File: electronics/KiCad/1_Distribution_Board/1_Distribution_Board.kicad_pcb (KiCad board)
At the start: 2 copper layers, 130 x 120 mm, 193 parts, among them CN1 HC-5264-3A, CN2 HC-5264-3A, J1 JST VH, J10 Generic 2.54mm, J11 Generic 2.54mm, J12 Conn_01x06, J13 Conn_01x10, J14 2.54-1*4P母, J15 2.54-1*4P母, J16 PM254V-11-06-H85, J17 Conn_02x08_Odd_Even, J18 PM254V-11-06-H85, J19 2.54-1*4P母, J2 JST VH, J20 2.54-1*4P母, J21 Jumper Pins, J22 Jumper Pins, J23 JST PH, J24 Generic 2.54mm, J25 Jumper Pins, J26 Jumper Pins, J27 JST PH, J28 Generic 2.54mm, J29 Jumper Pins, J3 JST VH, J30 Jumper Pins, J31 JST PH, J32 Generic 2.54mm, J33 Jumper Pins, J34 Jumper Pins, J35 JST PH, J36 Generic 2.54mm, J37 Jumper Pins, J38 Jumper Pins, J39 JST PH, J4 Conn_01x04, J40 Generic 2.54mm, J5 Generic 2.54mm, J6 Generic 2.54mm, J8 Generic 2.54mm, J9 Generic 2.54mm, M1 MountingHole_3.2mm_M3_ISO7380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, P1 Header-Female-2.54_1x8, P10 Header-Female-2.54_1x8, P11 Header-Female-2.54_1x2, P12 Header-Female-2.54_1x8, P13 Header-Female-2.54_1x8, P14 Header-Female-2.54_1x2, P15 Header-Female-2.54_1x8, P2 Header-Female-2.54_1x2, P3 Header-Female-2.54_1x8, P4 Header-Female-2.54_1x8, P5 Header-Female-2.54_1x2, P6 Header-Female-2.54_1x8, P7 Header-Female-2.54_1x8, P8 Header-Female-2.54_1x2, P9 Header-Female-2.54_1x8, Q1 DMG2305UX, Q2 AO3400A, Q3 AO3400A, Q4 AO3400A, Q5 AO3400A, U1 KH-2.54FH-1X20P-H8.5, U2 KH-2.54FH-1X20P-H8.5, U3 R-78C5.0-1.0, U4 R-78B12-2.0, U5 R-78B6.5-1.5, U6 PCA9306, U7 PCA9685PW, Y1 25MHz

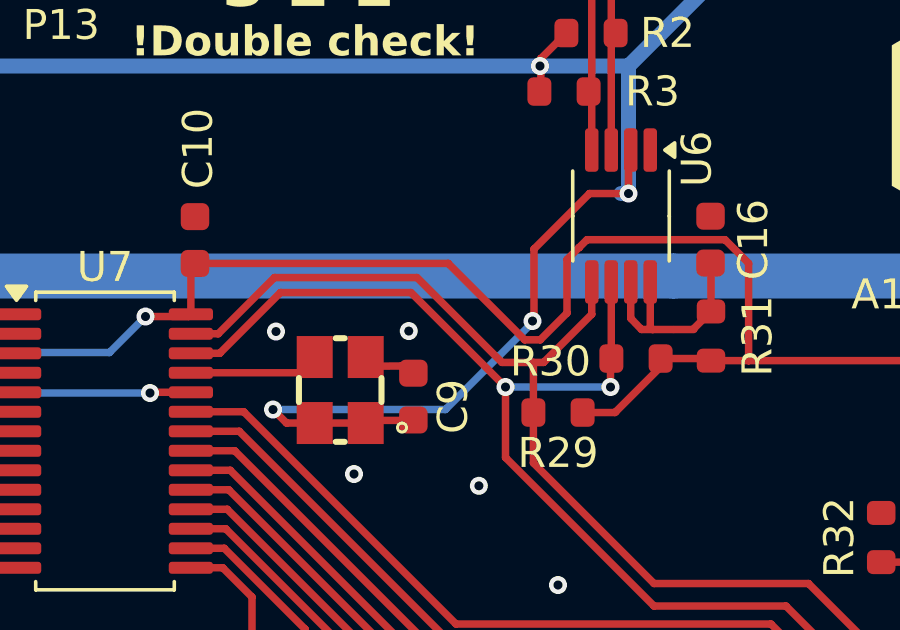
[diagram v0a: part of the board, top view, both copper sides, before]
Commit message: Fix Y1 oscillator supply routing and switch to 5V
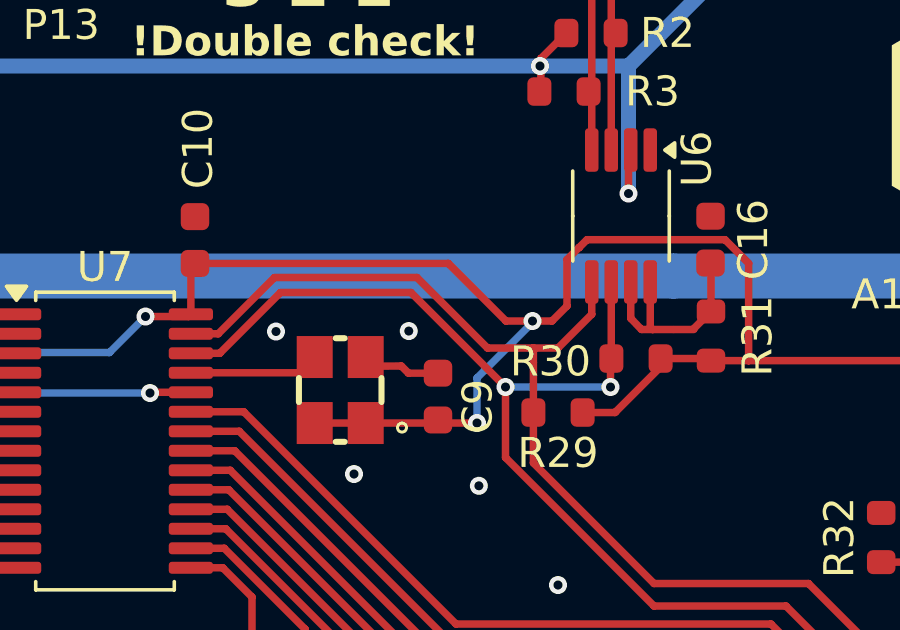
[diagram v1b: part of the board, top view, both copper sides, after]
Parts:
- moved C9 0.82 mm to (68.9, 98.5)
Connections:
- C9 pad 2: +3V3 -> VSYS
- Y1 pad 1: +3V3 -> VSYS
- Y1 pad 4: +3V3 -> VSYS
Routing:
- net +3V3: track 478.5 -> 456.8 mm, vias 19 -> 17
- net VSYS: track 170.5 -> 174.2 mm, vias 3 -> 5

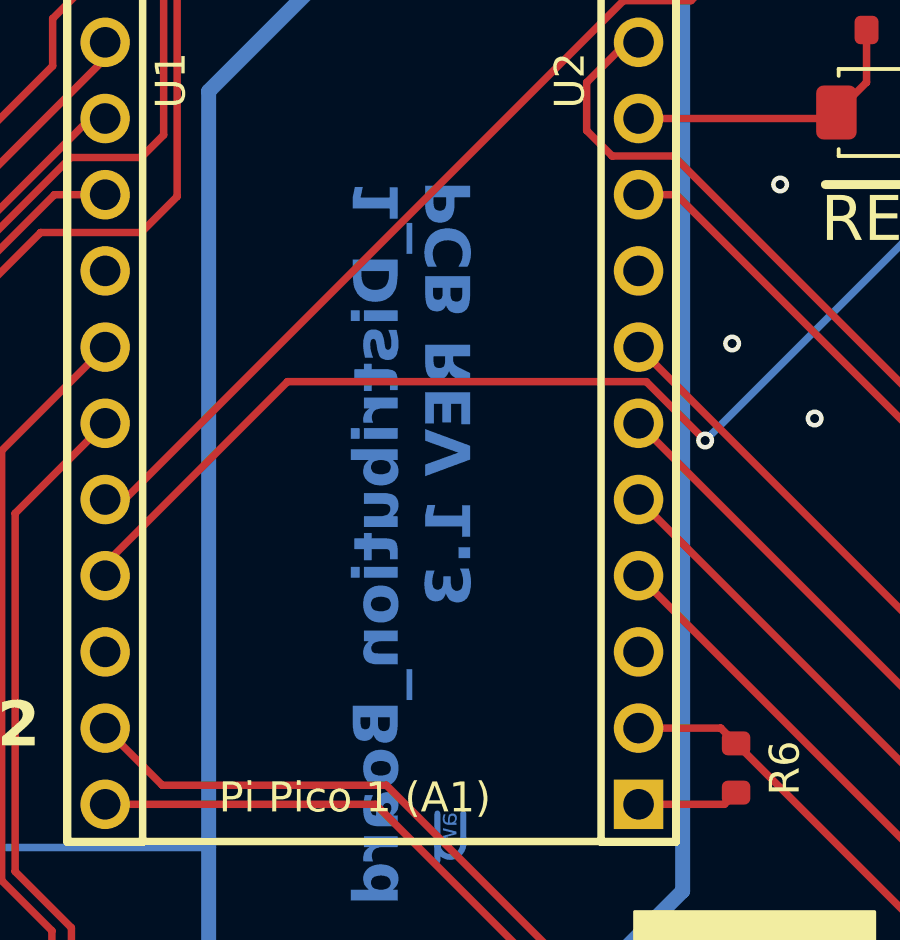
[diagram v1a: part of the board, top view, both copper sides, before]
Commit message: feat(electronics): update Distribution Board v1.3+ schematic and PCB layout
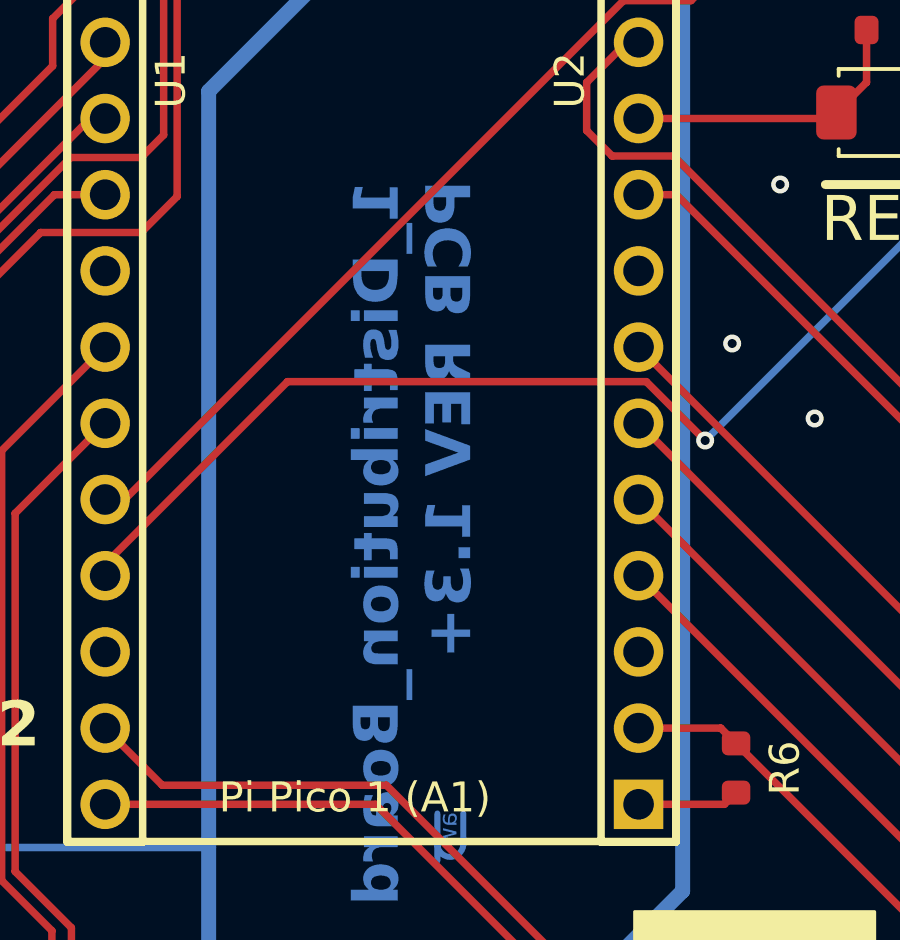
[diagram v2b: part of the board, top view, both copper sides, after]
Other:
- board text added: "1_Distribution_Board PCB REV 1.3+"
- board text removed: "1_Distribution_Board PCB REV 1.3"
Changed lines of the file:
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@@
 			(disableapertmacros no)
 			(usegerberextensions yes)
-			(usegerberattributes yes)
+			(usegerberattributes no)
 			(usegerberadvancedattributes yes)
 			(creategerberjobfile yes)
@@
 			(dashed_line_gap_ratio 3)
 			(svgprecision 4)
-			(plotframeref yes)
+			(plotframeref no)
 			(mode 1)
-			(useauxorigin yes)
+			(useauxorigin no)
 			(pdf_front_fp_property_popups yes)
 			(pdf_back_fp_property_popups yes)
@@
 			(drillshape 0)
 			(scaleselection 1)
-			(outputdirectory "1_Distribution_Board_Outputs/GerbersV1.1/")
+			(outputdirectory "production/v1.3+/")
 		)
 	)
@@
 			)
 		)
-		(attr smd dnp)
+		(attr smd)
 		(duplicate_pad_numbers_are_jumpers no)
 		(fp_line
@@
 		(layer "Edge.Cuts")
 	)
-	(gr_text "1_Distribution_Board\nPCB REV 1.3"
+	(gr_text "1_Distribution_Board\nPCB REV 1.3+"
 		(at 88.15 55 90)
 		(layer "B.Cu")
